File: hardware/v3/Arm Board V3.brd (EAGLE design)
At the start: 114.3 x 50.8 mm, 83 parts, among them CN1 1X4-BIG, IC1 L6208D, IC10 74LVC1G125DCK, IC2 L6208D, IC3 L6208D, IC4 LMV358IDGKR, IC5 NCP1117ST33T3G -3V3, IC6 ATMEGA16U2-MU, Q2 BC847BSMD, T1 FDN340P, T2 FDN340P, T3 FDN340P, U2 ST3485EBDR, U3 ATSAM3X8EA-AU, Y1 12MHz KX-7 20pF, Y2 32.768Khz, Y4 12MHz KX-7 20pF

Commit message: Expanded board
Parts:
- moved C20 131.2 mm to (87.6, 43.2)
- moved RN3 82.0 mm to (36.8, 14.1)
- moved L 82.0 mm to (33.4, 13.1)
- moved ON 82.0 mm to (33.4, 11.2)
- moved RX 82.0 mm to (33.4, 16.8)
- moved TX 82.0 mm to (33.4, 14.9)
- moved IC4 80.2 mm to (40.9, 14.0)
- moved C30 77.7 mm to (37.3, 11.0)
- moved T2 51.5 mm to (2.54, 37.5)
- moved T1 50.3 mm to (6.76, 37.6)
- moved C19 49.4 mm to (1.47, 33.9)
- moved R7 48.6 mm to (16.5, 47.7), turned to 0 degrees
- moved ERASE 48.1 mm to (12.9, 31.1)
- moved C25 45.7 mm to (17.0, 44.8), turned to 90 degrees
- moved C24 44.9 mm to (15.2, 43.3), turned to 90 degrees
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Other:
- board size 114.3 x 50.8 mm -> 114.3 x 76.2 mm

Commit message: XBEE
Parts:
- added U$1: XBEE-1B2, SparkFun-RF:XBEE-SILK
- moved C20 40.2 mm to (120.7, 66.0)
- moved RESET 40.2 mm to (120.7, 71.1)
- moved L 35.9 mm to (2.92, 32.1)
- moved C30 35.9 mm to (6.83, 30.1)
- moved IC4 35.9 mm to (10.5, 33.0)
- moved ON 35.9 mm to (2.92, 30.2)
- moved RX 35.9 mm to (2.92, 35.9)
- moved TX 35.9 mm to (2.92, 34.0)
- moved RN3 35.9 mm to (6.27, 33.2)
- moved JP7 22.7 mm to (91.4, 59.7), turned to 270 degrees
- moved CN1 19.0 mm to (91.4, 66.5), turned to 90 degrees
- moved U2 18.1 mm to (101.6, 69.8)
- moved IC5 15.3 mm to (85.2, 41.8), turned to 180 degrees
- moved C23 12.7 mm to (12.6, 56.0)
- moved C24 12.7 mm to (15.2, 56.0)
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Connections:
- new net VDD: U$1.1
- net GND: now also U$1.10
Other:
- board size 114.3 x 76.2 mm -> 127 x 76.2 mm

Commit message: stuff
Expanded the board
Binded EA pin to PWMs
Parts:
- moved U3 1.27 mm to (41.9, 36.8), turned to 90 degrees
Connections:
- net PWM5: now also IC2.14
- net PWM6: now also IC2.23
- net PWM7: now also IC3.23
- net PWM8: now also IC1.23
- net PWM9: now also IC1.14

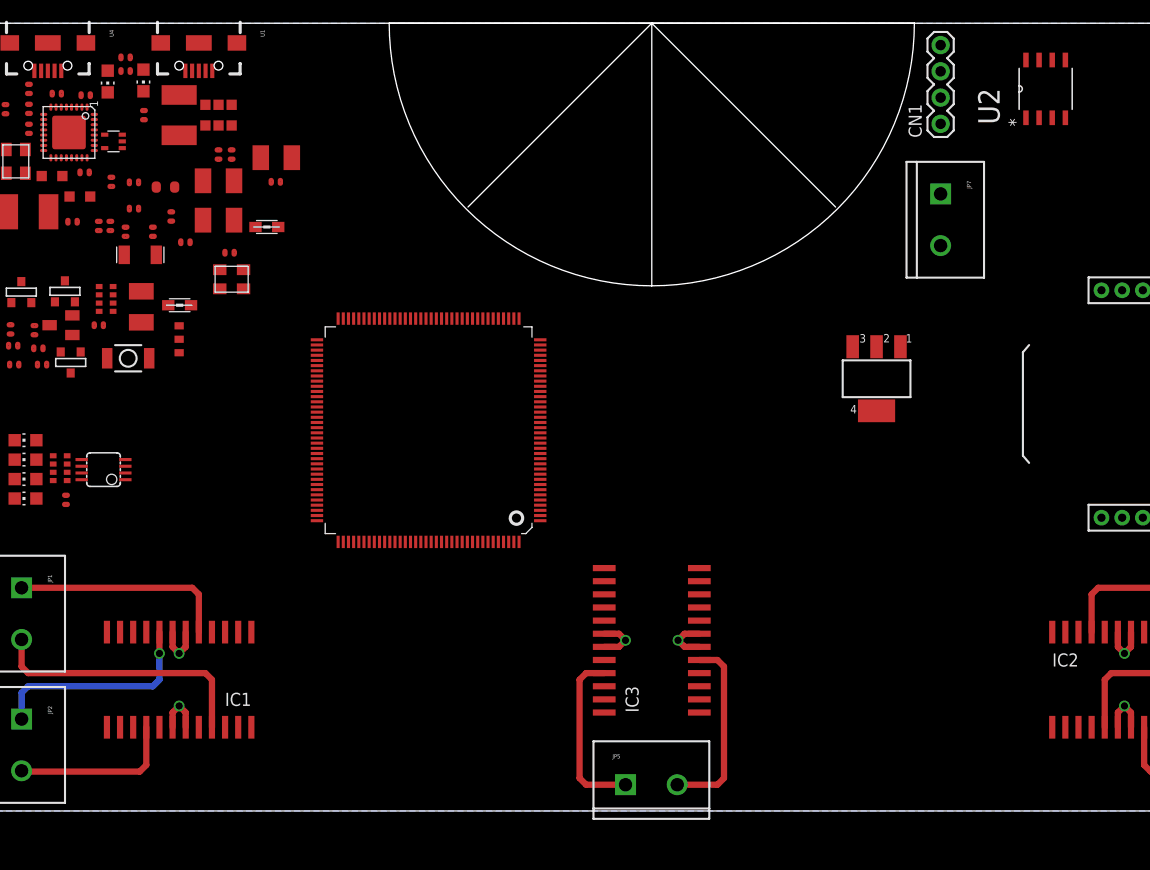
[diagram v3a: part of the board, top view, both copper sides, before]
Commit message: Connected motor controllers and Dynamixel
Bunch of stuff in the schematic
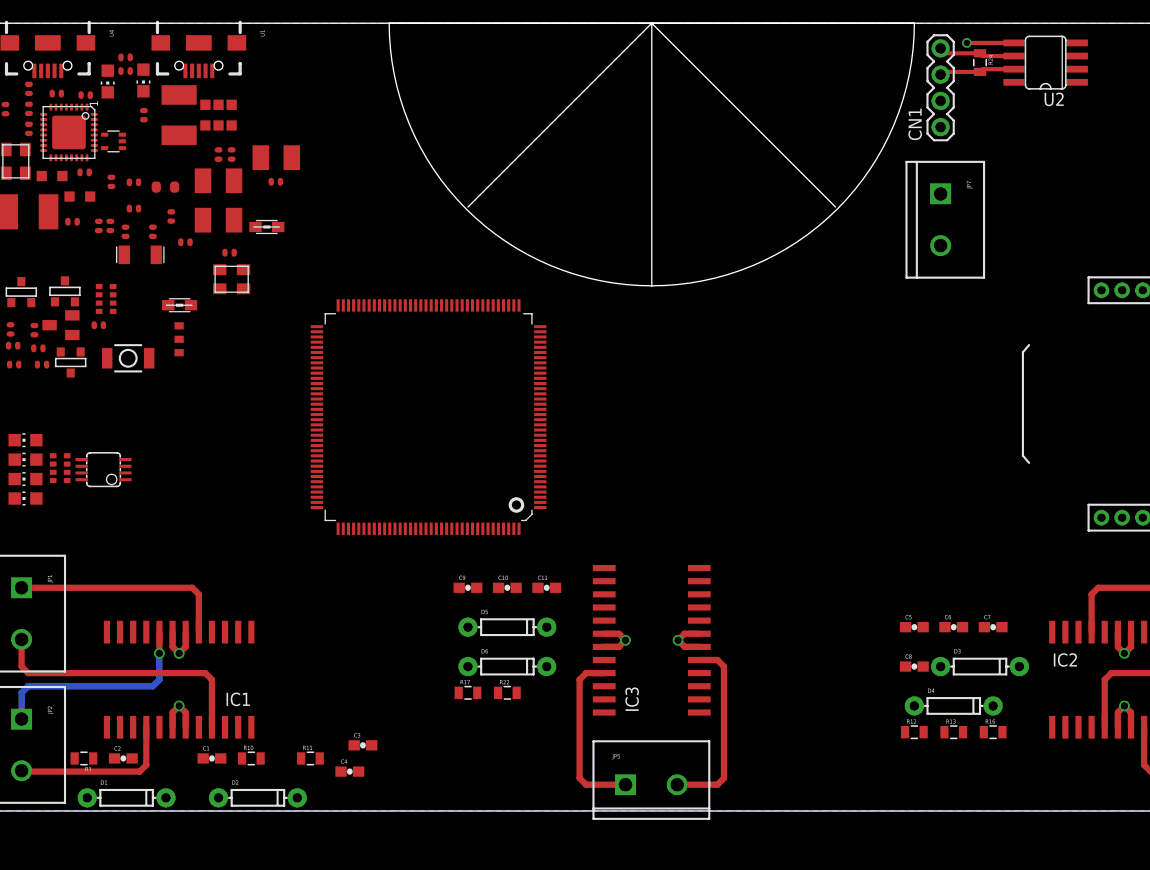
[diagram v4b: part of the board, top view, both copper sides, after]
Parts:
- removed C29: 10u, rcl:SMC_B
- removed C30: 100n, SmartPrj:C0402
- removed IC5: NCP1117ST33T3G -3V3, linear:SOT223
- added C1, C10, C11, C2, C3, C4, C5, C6, C7, C8, C9: 0.1uF, SparkFun-Capacitors:0603-CAP
- added D1, D2, D3, D4, D5, D6: (no value), SparkFun-DiscreteSemi:DIODE-1N4148
- added R1, R10, R11, R12, R13, R16, R17, R22: (no value), SparkFun-Passives:0805
- added R24: 220, SparkFun-Passives:0805
- U2: value ST3485EBDR -> MAX3468CSA; device ST Microelctronics_By_element14_Batch_1:SOIC127P600X175-8N -> maxim:SO08
- moved U2 2.54 mm to (101.6, 72.4)
- moved U3 1.27 mm to (41.9, 38.1)
- moved CN1 0.32 mm to (91.4, 66.1)
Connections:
- removed net VCC: U2.8
- new net +12V: CN1.2
- new net DD+: CN1.3, R24.2, U2.7
- new net DD-: CN1.4, R24.1, U2.6
- new net N$10: C8.2, R16.1
- new net N$13: C4.1, IC1.22
- new net N$15: C4.2, R11.1
- new net N$16: C8.1, IC2.22
- new net N$17: D5.C, D6.A, R22.2
- new net N$18: C11.2, R22.1
- new net N$19: C11.1, IC3.22
- new net N$8: D3.C, D4.A, R16.2
- new net N$9: D1.C, D2.A, R11.2
- new net OCD_A_1: C1.2, IC1.23, IC1.4, IC2.4, R10.1
- new net OCD_A_2: C5.2, IC2.23, R13.1
- new net OCD_A_3: C9.2, IC3.23, IC3.4, R17.1
- new net OCD_B_1: C2.1, IC1.14, IC1.9, R1.1
- new net OCD_B_2: C6.1, IC2.14, IC2.9, R12.1
- new net V+: IC4.8
- new net V-: IC4.4
- new net VBOOT_1: C3.2, D2.C, IC1.15
- new net VBOOT_2: C7.2, D4.C, IC2.15
- new net VBOOT_3: C10.2, D6.C, IC3.15
- new net VS: C10.1, C3.1, C7.1, D1.A, D3.A, D5.A, IC1.17, IC1.20, IC2.17, IC2.20, IC3.17, IC3.20
- net +3V3: no longer C29.+, IC5.2, IC5.4
- net +5V: now also U2.8; no longer C30.2, IC4.8, IC5.3
- net GND: now also C1.1, C2.2, C5.1, C6.2, C9.1, CN1.1, IC1.10, IC1.13, IC1.24, IC1.3, IC2.10, IC2.13, IC2.24, IC2.3, IC3.10, IC3.13, IC3.24, IC3.3, U2.5; no longer C29.-, C30.1, IC4.4, IC5.1
- net PIN23: now also U2.2, U2.3
- net PIN25: now also IC2.1
- net PIN26: now also IC2.2
- net PIN27: now also IC2.11
- net PIN28: now also IC2.12
- net PIN29: now also IC3.1
- net PIN30: now also IC3.2
- net PIN44: now also IC1.1
- net PIN45: now also IC1.2
- net PIN46: now also IC1.11
- net PIN47: now also IC1.12
- net PWM5: now also R13.2; no longer IC2.14
- net PWM6: now also R12.2; no longer IC2.23
- net PWM7: now also R17.2; no longer IC3.23
- net PWM8: now also R10.2; no longer IC1.23
- net PWM9: now also R1.2; no longer IC1.14
- net RXD1: now also U2.1
- net TXD1: now also U2.4
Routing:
- net DD-: track 0.00 -> 7.39 mm
- net DD+: track 0.00 -> 7.30 mm
- net GND: track 27.9 -> 32.4 mm, vias 6 -> 7

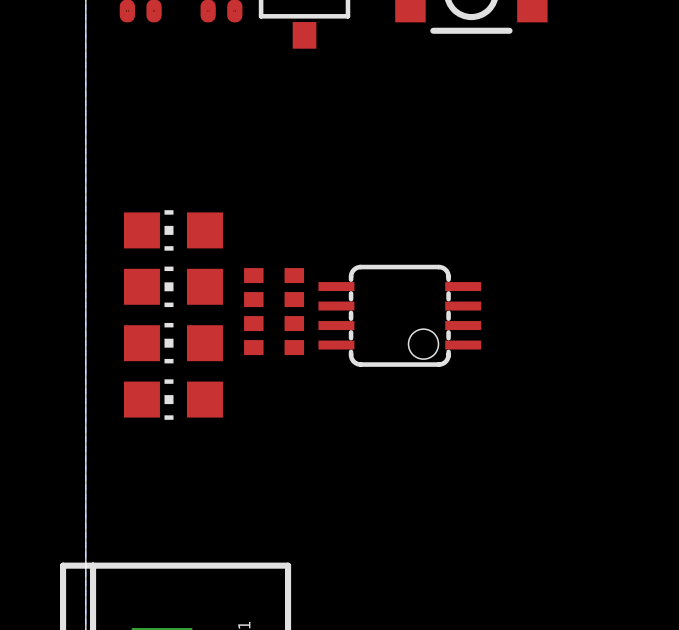
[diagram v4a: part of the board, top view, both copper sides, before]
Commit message: Added Xbee connections to schematic
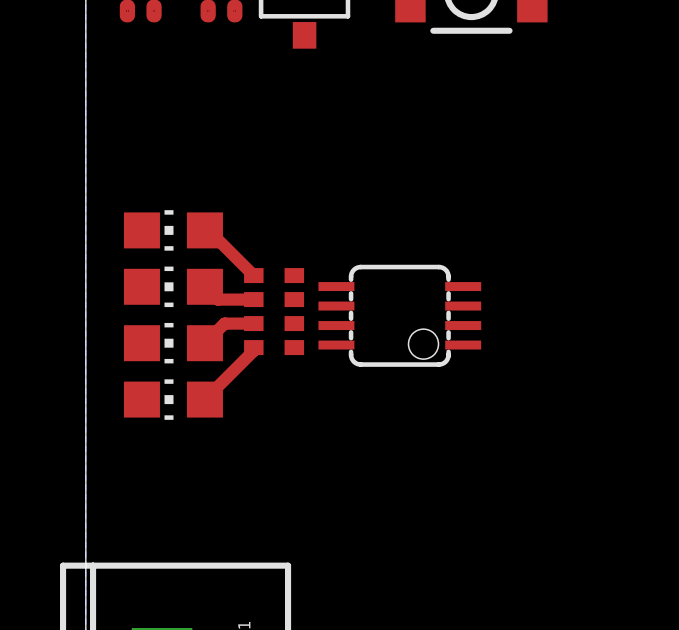
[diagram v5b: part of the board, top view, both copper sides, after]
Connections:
- removed net VDD: U$1.1
- net +5V: now also U$1.1
- net RXD2: now also U$1.2
- net TXD2: now also U$1.3
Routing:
- net N$3: track 0.00 -> 2.41 mm
- net N$54: track 0.00 -> 2.25 mm
- net N$2: track 0.00 -> 1.90 mm
- net N$55: track 0.00 -> 1.80 mm
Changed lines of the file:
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@@
 <layers>
 <layer number="1" name="Top" color="4" fill="1" visible="yes" active="yes"/>
+<layer number="2" name="Route2" color="1" fill="3" visible="yes" active="yes"/>
 <layer number="3" name="Route3" color="4" fill="3" visible="no" active="no"/>
 <layer number="4" name="Route4" color="1" fill="4" visible="no" active="no"/>
@@
 <layer number="13" name="Route13" color="4" fill="5" visible="no" active="no"/>
 <layer number="14" name="Route14" color="1" fill="6" visible="no" active="no"/>
+<layer number="15" name="Route15" color="4" fill="6" visible="yes" active="yes"/>
 <layer number="16" name="Bottom" color="1" fill="1" visible="yes" active="yes"/>
 <layer number="17" name="Pads" color="2" fill="1" visible="yes" active="yes"/>
@@
 <contactref element="U1" pad="GND1"/>
 <contactref element="U4" pad="GND1"/>
-<contactref element="U$1" pad="10"/>
 <contactref element="IC1" pad="3"/>
 <contactref element="IC1" pad="10"/>
@@
 <wire x1="98.5266" y1="74.295" x2="93.98" y2="74.295" width="0.4064" layer="1"/>
 <via x="93.98" y="74.295" extent="1-16" drill="0.6" shape="octagon"/>
+<contactref element="U$1" pad="10"/>
 <wire x1="116.45" y1="73.37" x2="124.85" y2="73.37" width="0" layer="19" extent="1-1"/>
 <wire x1="98.5266" y1="74.295" x2="116.45" y2="73.37" width="0" layer="19" extent="1-1"/>
@@
 <contactref element="T2" pad="2"/>
 <contactref element="U2" pad="8"/>
+<contactref element="U$1" pad="1"/>
+<wire x1="107" y1="28.37" x2="98.5266" y2="70.485" width="0" layer="19" extent="1-1"/>
 <wire x1="13.0429" y1="71.5772" x2="98.5266" y2="70.485" width="0" layer="19" extent="1-1"/>
 <wire x1="12.1539" y1="72.898" x2="13.0429" y2="71.5772" width="0" layer="19" extent="1-1"/>
@@
 <contactref element="ON" pad="A"/>
 <contactref element="RN3" pad="4"/>
-<wire x1="3.971" y1="30.226" x2="5.5988" y2="31.9597" width="0" layer="19" extent="1-1"/>
+<wire x1="5.5988" y1="31.9597" x2="5.5988" y2="31.8538" width="0.4064" layer="1"/>
+<wire x1="5.5988" y1="31.8538" x2="3.971" y2="30.226" width="0.4064" layer="1"/>
 </signal>
 <signal name="+3V3">
@@
 <contactref element="RX" pad="A"/>
 <contactref element="RN3" pad="1"/>
-<wire x1="5.5988" y1="34.3597" x2="3.971" y2="35.8648" width="0" layer="19" extent="1-1"/>
+<wire x1="3.971" y1="35.8648" x2="4.0937" y2="35.8648" width="0.4064" layer="1"/>
+<wire x1="4.0937" y1="35.8648" x2="5.5988" y2="34.3597" width="0.4064" layer="1"/>
 </signal>
 <signal name="N$55">
 <contactref element="TX" pad="A"/>
 <contactref element="RN3" pad="2"/>
-<wire x1="3.971" y1="33.9852" x2="5.5988" y2="33.5597" width="0" layer="19" extent="1-1"/>
+<wire x1="5.5988" y1="33.5597" x2="4.3965" y2="33.5597" width="0.4064" layer="1"/>
+<wire x1="4.3965" y1="33.5597" x2="3.971" y2="33.9852" width="0.4064" layer="1"/>
 </signal>
 <signal name="USBVCC">
@@
 <contactref element="L" pad="A"/>
 <contactref element="RN3" pad="3"/>
-<wire x1="3.971" y1="32.1056" x2="5.5988" y2="32.7597" width="0" layer="19" extent="1-1"/>
+<wire x1="5.5988" y1="32.7597" x2="4.6251" y2="32.7597" width="0.4064" layer="1"/>
+<wire x1="4.6251" y1="32.7597" x2="3.971" y2="32.1056" width="0.4064" layer="1"/>
 </signal>
 <signal name="GATE_CMD">
@@
 <signal name="TXD2">
 <contactref element="U3" pad="4"/>
+<contactref element="U$1" pad="3"/>
+<wire x1="52.71" y1="30.85" x2="111" y2="28.37" width="0" layer="19" extent="1-1"/>
 </signal>
 <signal name="SDA1">
@@
 <signal name="RXD2">
 <contactref element="U3" pad="3"/>
+<contactref element="U$1" pad="2"/>
+<wire x1="52.71" y1="30.35" x2="109" y2="28.37" width="0" layer="19" extent="1-1"/>
 </signal>
 <signal name="AD14(RXD3)">
@@
 <wire x1="2.5146" y1="51.2064" x2="5.1504" y2="57.9628" width="0" layer="19" extent="1-1"/>
 </signal>
-<signal name="VDD">
-<contactref element="U$1" pad="1"/>
-</signal>
 <signal name="OCD_B_1">
